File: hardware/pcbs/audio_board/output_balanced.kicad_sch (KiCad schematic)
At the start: 13 parts, among them J9 NC3MAH, U6 TL072

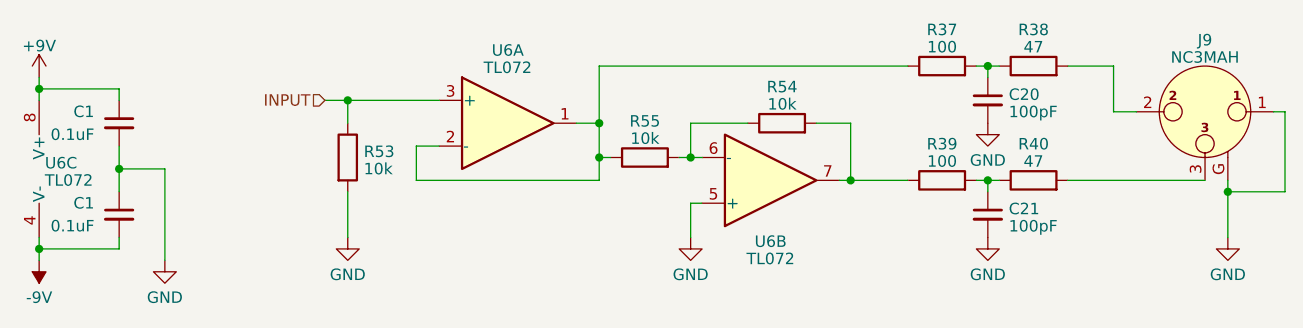
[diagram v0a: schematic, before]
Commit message: Small audio board fixes and add DHAN-M module
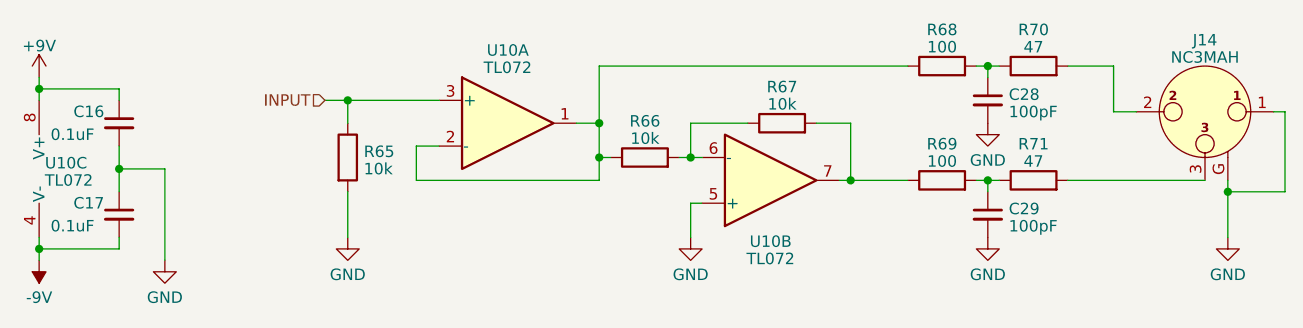
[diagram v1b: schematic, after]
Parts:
- renumbered C1 to C16, C1 to C17, C20 to C28, C21 to C29, J9 to J14, R53 to R65, R55 to R66, R54 to R67, R37 to R68, R39 to R69, R38 to R70, R40 to R71, U6 to U10
